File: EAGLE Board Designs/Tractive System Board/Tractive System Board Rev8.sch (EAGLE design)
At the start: 116 parts, among them J1 CONNECTOR-5_MICRO_V7S_, J2 CONNECTOR-5_MICRO_V6S_, J3 CONNECTOR-8_μF_T_V_BLACK, K1 RELAY_SPST_NO_D_24, Q2 TRANSISTOR_N_MOS__PMV15ENEA, U10 LTC6994-2, U5 RELAY_SOLIDSTATE_NO_AB38S-Q-A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, U6 LT8315, U7 AMC3330_AIRGAP, U8 AMC3330_AIRGAP

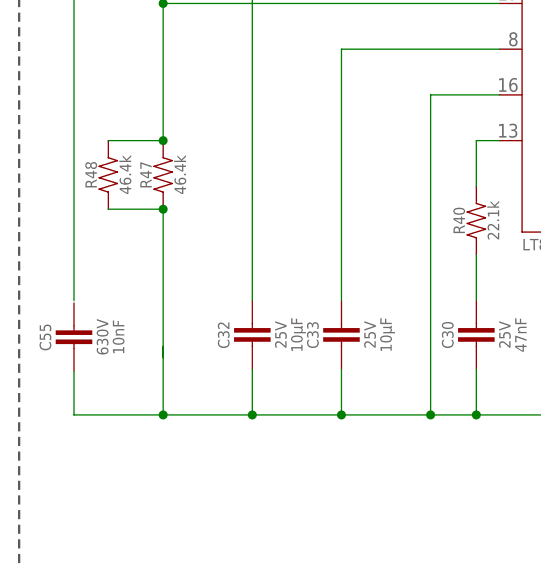
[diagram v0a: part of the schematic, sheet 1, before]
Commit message: tsb-rev8 update
fixed net bugs
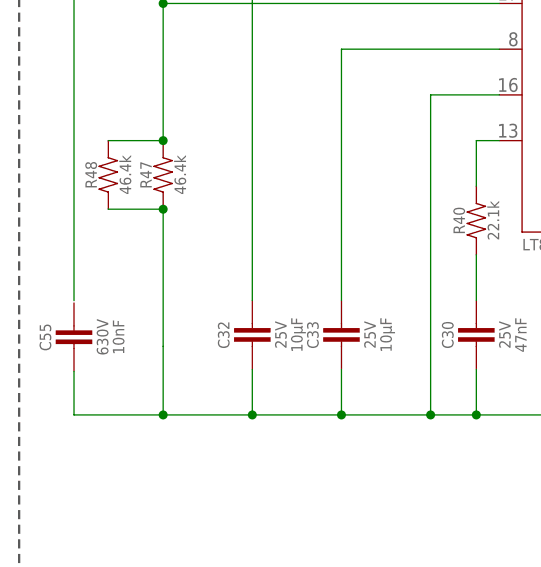
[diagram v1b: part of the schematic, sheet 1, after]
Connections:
- removed net N$37: R47.1, R48.1
- net TS-FUSED1: now also R47.1, R48.1
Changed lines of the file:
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@@
 <pinref part="C55" gate="G$1" pin="2"/>
 <pinref part="C56" gate="G$1" pin="2"/>
+<pinref part="R48" gate="G$1" pin="1"/>
+<pinref part="R47" gate="G$1" pin="1"/>
+<wire x1="17.526" y1="129.54" x2="23.622" y2="129.54" width="0.6096" layer="91"/>
+<wire x1="23.622" y1="129.54" x2="23.622" y2="114.3" width="0.6096" layer="91"/>
+<junction x="23.622" y="129.54"/>
 </segment>
 </net>
@@
 </segment>
 </net>
-<net name="N$37" class="0">
-<segment>
-<pinref part="R48" gate="G$1" pin="1"/>
-<pinref part="R47" gate="G$1" pin="1"/>
-<wire x1="23.622" y1="129.54" x2="17.526" y2="129.54" width="0.6096" layer="91"/>
-<junction x="23.622" y="129.54"/>
-<wire x1="23.622" y1="129.54" x2="23.622" y2="113.03" width="0.6096" layer="91"/>
-</segment>
-</net>

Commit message: tsb-rev8 buck layout
part placement of key buck converter topology
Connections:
- net N$36 renamed IREG/SS
- net N$41 renamed VC
- net N$45 renamed INTVCC
- net N$47 renamed SOURCE
- net N$54 renamed FB
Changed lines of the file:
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@@
 </segment>
 </net>
-<net name="N$36" class="0">
+<net name="IREG/SS" class="0">
 <segment>
 <pinref part="U6" gate="G$1" pin="IREG/SS"/>
@@
 </segment>
 </net>
-<net name="N$41" class="0">
+<net name="VC" class="0">
 <segment>
 <pinref part="U6" gate="G$1" pin="VC"/>
@@
 </segment>
 </net>
-<net name="N$47" class="0">
+<net name="SOURCE" class="0">
 <segment>
 <pinref part="U6" gate="G$1" pin="SOURCE"/>
@@
 </segment>
 </net>
-<net name="N$54" class="0">
+<net name="FB" class="0">
 <segment>
 <pinref part="U6" gate="G$1" pin="FB"/>
@@
 </segment>
 </net>
-<net name="N$45" class="0">
+<net name="INTVCC" class="0">
 <segment>
 <pinref part="C33" gate="G$1" pin="1"/>

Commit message: tsb-rev8-schematic-update
Added, DNP resistor for connecting EN/UVLO to INTVCC in the case that we don't want to use selective 60V chip activation
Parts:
- added R1: RESISTOR_0603_DNP, HyTechDevices:RESISTOR_0603_DNP
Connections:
- net EN/UVLO: now also R1.2
- net INTVCC: now also R1.1
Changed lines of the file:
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@@
 <part name="R56" library="HyTechDevices" deviceset="RESISTOR_?_*" device="1206" technology="HV4.99K"/>
 <part name="R61" library="HyTechDevices" deviceset="RESISTOR_?_*" device="1206" technology="HV4.99K"/>
+<part name="R1" library="HyTechDevices" deviceset="RESISTOR_?_*" device="0603" technology="DNP"/>
 </parts>
 <sheets>
@@
 <attribute name="NAME" x="62.23" y="181.61" size="1.27" layer="95" align="bottom-center"/>
 <attribute name="RESISTANCE" x="62.23" y="179.07" size="1.27" layer="96" align="top-center"/>
+</instance>
+<instance part="R1" gate="G$1" x="37.592" y="101.092" smashed="yes" rot="R180">
+<attribute name="NAME" x="38.862" y="99.822" size="1.27" layer="95" rot="R180" align="bottom-center"/>
+<attribute name="RESISTANCE" x="38.862" y="102.362" size="1.27" layer="96" rot="R180" align="top-center"/>
 </instance>
 </instances>
@@
 <label x="48.26" y="162.56" size="1.27" layer="95" xref="yes"/>
 </segment>
+<segment>
+<pinref part="R1" gate="G$1" pin="2"/>
+<wire x1="35.052" y1="101.092" x2="32.512" y2="101.092" width="0.6096" layer="91"/>
+<label x="32.512" y="101.092" size="1.27" layer="95" rot="R180" xref="yes"/>
+</segment>
 </net>
 <net name="IREG/SS" class="0">
@@
 <pinref part="U6" gate="G$1" pin="INTVCC"/>
 </segment>
-</net>
+<segment>
+<pinref part="R1" gate="G$1" pin="1"/>
+<wire x1="42.672" y1="101.092" x2="45.212" y2="101.092" width="0.6096" layer="91"/>
+<label x="45.212" y="101.092" size="1.27" layer="95" xref="yes"/>
+</segment>
+</net>

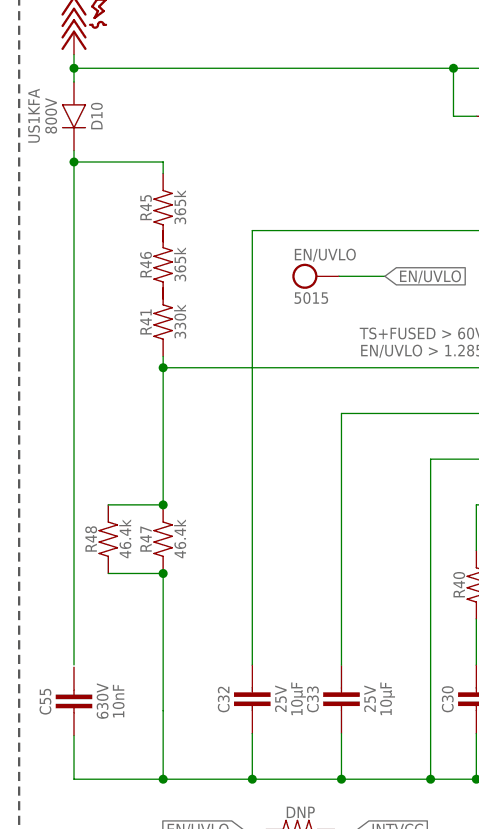
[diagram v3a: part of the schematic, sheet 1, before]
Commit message: tsb-rev8-layout-update
Fixed net issue to CAP 55. Finetuned buck parts placement, started initial routing
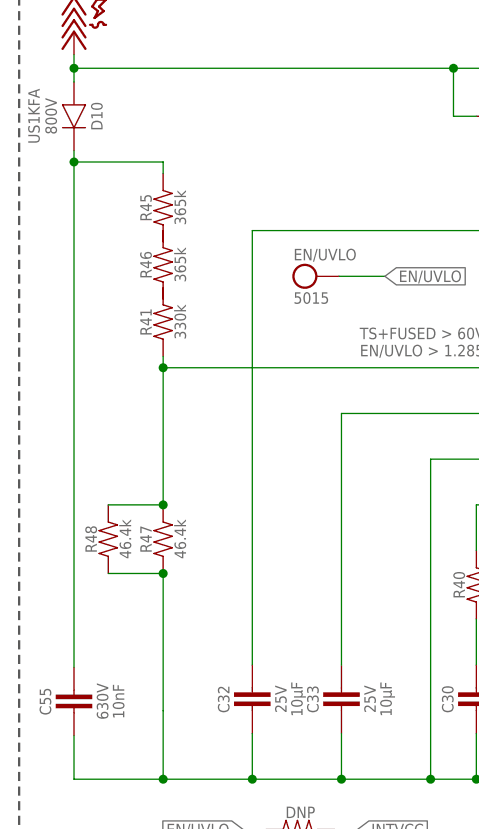
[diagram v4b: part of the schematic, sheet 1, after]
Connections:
- net N$46: now also C55.1
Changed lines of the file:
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@@
 <pinref part="D10" gate="G$1" pin="C"/>
 <wire x1="13.716" y1="176.53" x2="13.716" y2="175.26" width="0.6096" layer="91"/>
-<wire x1="13.716" y1="175.26" x2="13.716" y2="119.38" width="0.6096" layer="91"/>
 <wire x1="13.716" y1="175.26" x2="23.622" y2="175.26" width="0.6096" layer="91"/>
-<junction x="13.716" y="175.26"/>
 <pinref part="R45" gate="G$1" pin="2"/>
 <wire x1="23.622" y1="175.26" x2="23.622" y2="173.99" width="0.6096" layer="91"/>
+<pinref part="C55" gate="G$1" pin="1"/>
+<wire x1="13.716" y1="175.26" x2="13.716" y2="119.126" width="0.6096" layer="91"/>
+<junction x="13.716" y="175.26"/>
 </segment>
 </net>

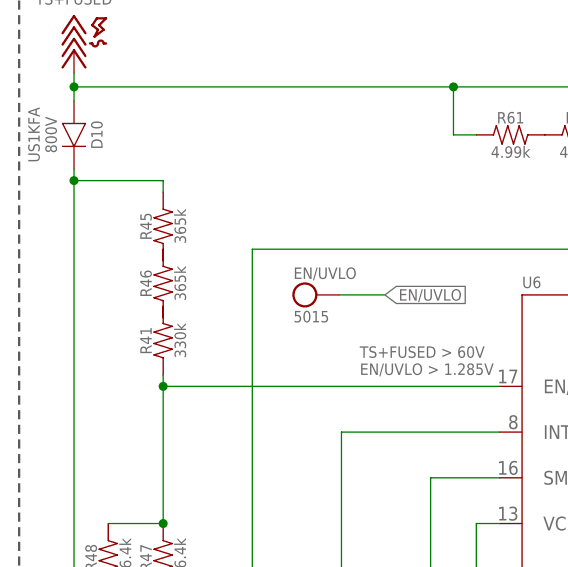
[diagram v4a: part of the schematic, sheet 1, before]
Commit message: tsb-rev8-layout-update
redid board dimensions
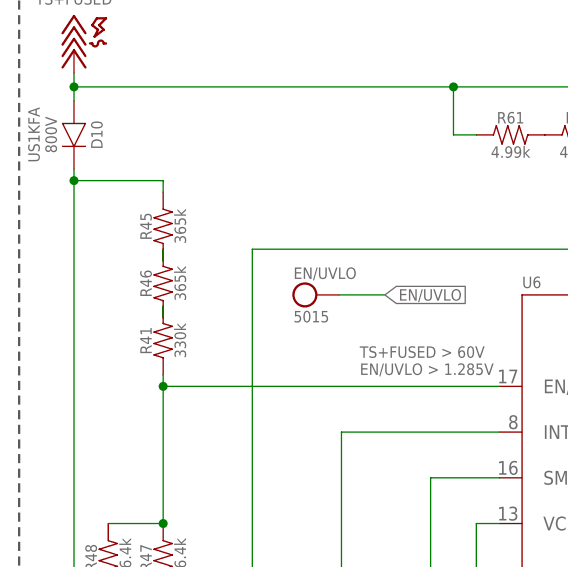
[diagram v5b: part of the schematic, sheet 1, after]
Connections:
- new net N$1: R41.2, R46.1
- new net N$4: R45.1, R46.2
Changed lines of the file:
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@@
+</segment>
+</net>
+<net name="N$1" class="0">
+<segment>
+<pinref part="R46" gate="G$1" pin="1"/>
+<pinref part="R41" gate="G$1" pin="2"/>
+<wire x1="23.622" y1="160.02" x2="23.622" y2="161.29" width="0.1524" layer="91"/>
+</segment>
+</net>
+<net name="N$4" class="0">
+<segment>
+<pinref part="R45" gate="G$1" pin="1"/>
+<pinref part="R46" gate="G$1" pin="2"/>
+<wire x1="23.622" y1="166.37" x2="23.622" y2="167.64" width="0.1524" layer="91"/>
 </segment>
 </net>

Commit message: tsb-rev8-layout-update
updated amc3330 routing with no NC and parts placement of en/uvlo resistor network. reconsidering placement of ts- fuse and connector
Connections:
- net TS-FUSED: no longer U7.NC, U8.NC
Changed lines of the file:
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@@
 <pinref part="U$28" gate="G$1" pin="TS-FUSED"/>
 <junction x="143.002" y="163.83"/>
-<wire x1="182.88" y1="154.94" x2="172.72" y2="154.94" width="0.6096" layer="91"/>
+<wire x1="186.69" y1="154.94" x2="172.72" y2="154.94" width="0.6096" layer="91"/>
 <wire x1="172.72" y1="154.94" x2="162.56" y2="154.94" width="0.6096" layer="91"/>
 <wire x1="162.56" y1="154.94" x2="157.48" y2="154.94" width="0.6096" layer="91"/>
-<pinref part="U7" gate="G$1" pin="NC"/>
-<wire x1="186.69" y1="180.34" x2="182.88" y2="180.34" width="0.6096" layer="91"/>
-<wire x1="182.88" y1="180.34" x2="182.88" y2="154.94" width="0.6096" layer="91"/>
-<junction x="182.88" y="154.94"/>
 <pinref part="C39" gate="G$1" pin="2"/>
 <wire x1="162.56" y1="156.21" x2="162.56" y2="154.94" width="0.6096" layer="91"/>
@@
 <junction x="172.72" y="154.94"/>
 <pinref part="U7" gate="G$1" pin="HGND"/>
-<wire x1="182.88" y1="154.94" x2="186.69" y2="154.94" width="0.6096" layer="91"/>
 <wire x1="186.69" y1="154.94" x2="186.69" y2="160.02" width="0.6096" layer="91"/>
 <pinref part="U7" gate="G$1" pin="DCDC_HGND"/>
@@
 <pinref part="U$31" gate="G$1" pin="TS-FUSED"/>
 <junction x="143.002" y="115.57"/>
-<wire x1="182.88" y1="106.68" x2="172.72" y2="106.68" width="0.6096" layer="91"/>
+<wire x1="186.69" y1="106.68" x2="172.72" y2="106.68" width="0.6096" layer="91"/>
 <wire x1="172.72" y1="106.68" x2="162.56" y2="106.68" width="0.6096" layer="91"/>
 <wire x1="162.56" y1="106.68" x2="157.48" y2="106.68" width="0.6096" layer="91"/>
-<pinref part="U8" gate="G$1" pin="NC"/>
-<wire x1="186.69" y1="132.08" x2="182.88" y2="132.08" width="0.6096" layer="91"/>
-<wire x1="182.88" y1="132.08" x2="182.88" y2="106.68" width="0.6096" layer="91"/>
-<junction x="182.88" y="106.68"/>
 <pinref part="C48" gate="G$1" pin="2"/>
 <wire x1="162.56" y1="107.95" x2="162.56" y2="106.68" width="0.6096" layer="91"/>
@@
 <junction x="172.72" y="106.68"/>
 <pinref part="U8" gate="G$1" pin="HGND"/>
-<wire x1="182.88" y1="106.68" x2="186.69" y2="106.68" width="0.6096" layer="91"/>
 <wire x1="186.69" y1="106.68" x2="186.69" y2="111.76" width="0.6096" layer="91"/>
 <pinref part="U8" gate="G$1" pin="DCDC_HGND"/>

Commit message: tsb-rev8-schematic-update
renamed lt8315 GND to PGND
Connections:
- net TS-FUSED1 renamed PGND
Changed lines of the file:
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@@
 </busses>
 <nets>
-<net name="TS-FUSED1" class="0">
+<net name="PGND" class="0">
 <segment>
 <pinref part="C33" gate="G$1" pin="2"/>

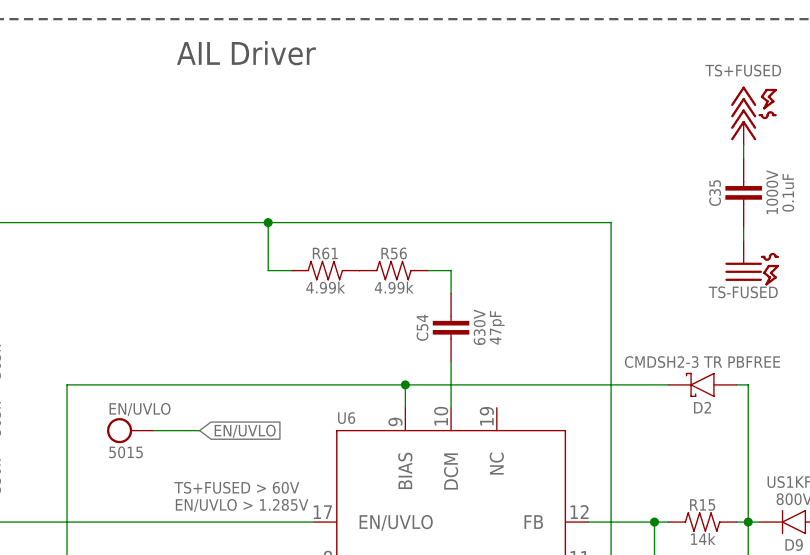
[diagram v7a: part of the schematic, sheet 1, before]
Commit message: tsb-rev8-layout-update
more buck routing
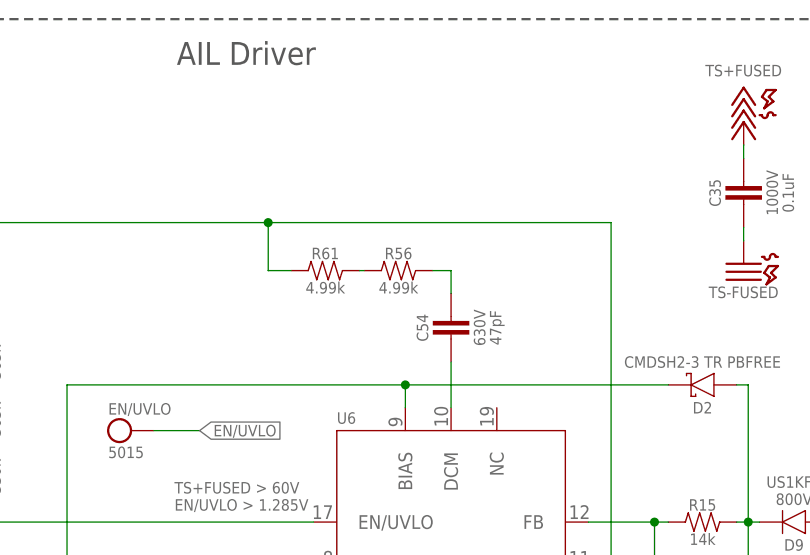
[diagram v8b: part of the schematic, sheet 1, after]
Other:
- moved on the sheet: R56
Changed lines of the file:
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@@
 <attribute name="CAPACITANCE" x="123.698" y="97.79" size="1.27" layer="96" rot="R90" align="top-center"/>
 </instance>
-<instance part="R56" gate="G$1" x="71.12" y="180.34" smashed="yes">
-<attribute name="NAME" x="69.85" y="181.61" size="1.27" layer="95" align="bottom-center"/>
-<attribute name="RESISTANCE" x="69.85" y="179.07" size="1.27" layer="96" align="top-center"/>
+<instance part="R56" gate="G$1" x="71.628" y="180.34" smashed="yes">
+<attribute name="NAME" x="70.358" y="181.61" size="1.27" layer="95" align="bottom-center"/>
+<attribute name="RESISTANCE" x="70.358" y="179.07" size="1.27" layer="96" align="top-center"/>
 </instance>
 <instance part="R61" gate="G$1" x="63.5" y="180.34" smashed="yes">
@@
 <pinref part="R56" gate="G$1" pin="1"/>
 <pinref part="R61" gate="G$1" pin="2"/>
+<wire x1="66.548" y1="180.34" x2="66.04" y2="180.34" width="0.1524" layer="91"/>
 </segment>
 </net>
@@
 <pinref part="R56" gate="G$1" pin="2"/>
 <pinref part="C54" gate="G$1" pin="1"/>
-<wire x1="73.66" y1="180.34" x2="76.2" y2="180.34" width="0.6096" layer="91"/>
+<wire x1="74.168" y1="180.34" x2="76.2" y2="180.34" width="0.6096" layer="91"/>
 <wire x1="76.2" y1="180.34" x2="76.2" y2="177.8" width="0.6096" layer="91"/>
 </segment>
